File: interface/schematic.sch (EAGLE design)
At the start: 31 parts, among them J1 AUDIO_JACK_3.5MM_KIT, J2 AUDIO_JACK_3.5MM_KIT, J3 RJ45, T1 2N3904, T2 2N3904

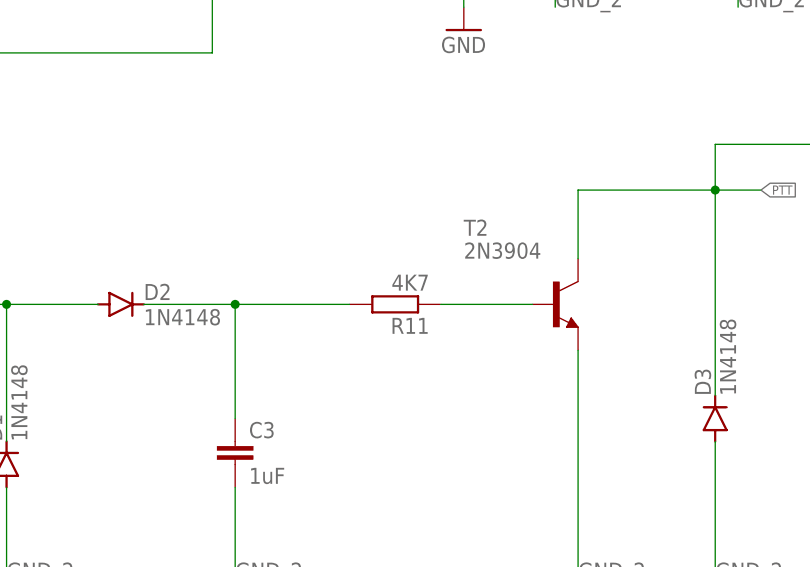
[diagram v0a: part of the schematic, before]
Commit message: Added decals
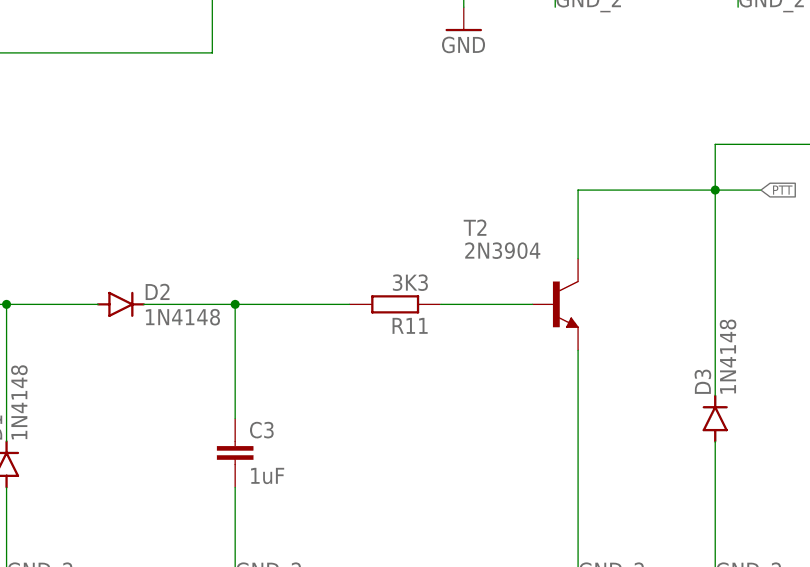
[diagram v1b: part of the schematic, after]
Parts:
- R11: value 4K7 -> 3K3
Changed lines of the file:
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@@
 <part name="R9" library="rcl" library_urn="urn:adsk.eagle:library:334" deviceset="R-EU_" device="0207/10" package3d_urn="urn:adsk.eagle:package:23491/2" value="330K"/>
 <part name="R10" library="rcl" library_urn="urn:adsk.eagle:library:334" deviceset="R-EU_" device="0207/10" package3d_urn="urn:adsk.eagle:package:23491/2" value="4K7"/>
-<part name="R11" library="rcl" library_urn="urn:adsk.eagle:library:334" deviceset="R-EU_" device="0207/10" package3d_urn="urn:adsk.eagle:package:23491/2" value="4K7"/>
+<part name="R11" library="rcl" library_urn="urn:adsk.eagle:library:334" deviceset="R-EU_" device="0207/10" package3d_urn="urn:adsk.eagle:package:23491/2" value="3K3"/>
 <part name="R13" library="rcl" library_urn="urn:adsk.eagle:library:334" deviceset="R-EU_" device="0207/10" package3d_urn="urn:adsk.eagle:package:23491/2" value="4k7"/>
 <part name="R5" library="rcl" library_urn="urn:adsk.eagle:library:334" deviceset="R-EU_" device="0207/10" package3d_urn="urn:adsk.eagle:package:23491/2" value="680R"/>

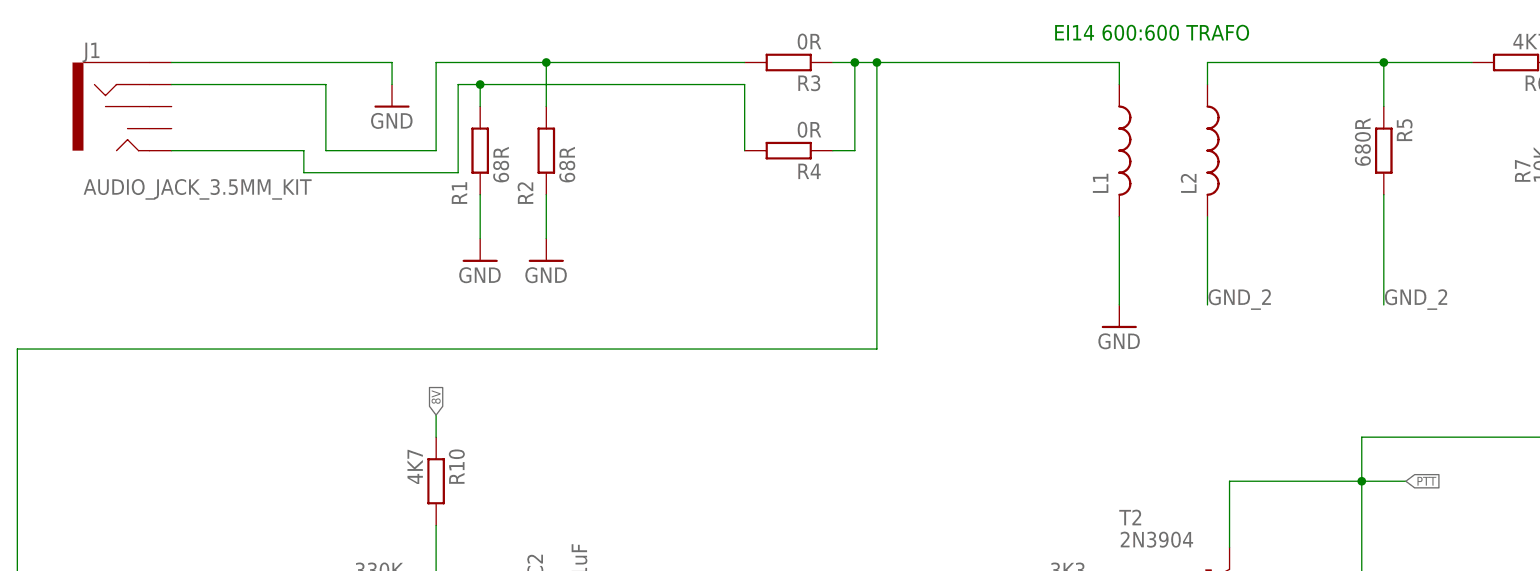
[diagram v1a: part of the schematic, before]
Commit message: Fixed component numbering to match ordered boards
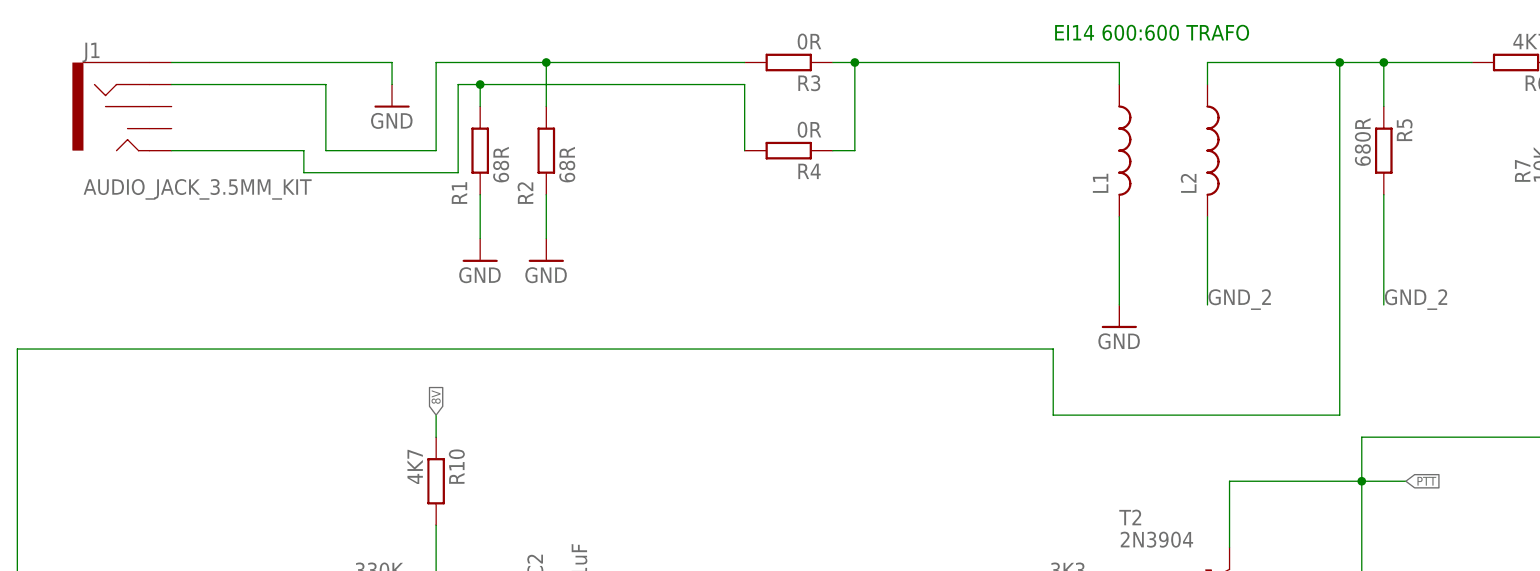
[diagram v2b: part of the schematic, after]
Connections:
- removed net N$8: L2.1, R5.1, R6.2
- new net N$16: L1.1, R3.1, R4.1
- net N$15: now also L2.1, R5.1, R6.2; no longer L1.1, R3.1, R4.1
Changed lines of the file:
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@@
-</segment>
-</net>
-<net name="N$8" class="0">
-<segment>
-<pinref part="L2" gate="G$1" pin="1"/>
-<wire x1="142.24" y1="167.64" x2="142.24" y2="170.18" width="0.1524" layer="91"/>
-<wire x1="142.24" y1="170.18" x2="162.56" y2="170.18" width="0.1524" layer="91"/>
-<pinref part="R6" gate="G$1" pin="2"/>
-<pinref part="R5" gate="G$1" pin="1"/>
-<wire x1="162.56" y1="170.18" x2="172.72" y2="170.18" width="0.1524" layer="91"/>
-<wire x1="162.56" y1="165.1" x2="162.56" y2="170.18" width="0.1524" layer="91"/>
-<junction x="162.56" y="170.18"/>
 </segment>
 </net>
@@
 <net name="N$15" class="0">
 <segment>
-<pinref part="L1" gate="G$1" pin="1"/>
-<wire x1="132.08" y1="170.18" x2="132.08" y2="167.64" width="0.1524" layer="91"/>
-<pinref part="R3" gate="G$1" pin="1"/>
-<wire x1="99.06" y1="170.18" x2="101.6" y2="170.18" width="0.1524" layer="91"/>
-<wire x1="101.6" y1="170.18" x2="104.14" y2="170.18" width="0.1524" layer="91"/>
-<pinref part="R4" gate="G$1" pin="1"/>
-<wire x1="99.06" y1="160.02" x2="101.6" y2="160.02" width="0.1524" layer="91"/>
-<wire x1="101.6" y1="160.02" x2="101.6" y2="170.18" width="0.1524" layer="91"/>
-<junction x="101.6" y="170.18"/>
-<wire x1="104.14" y1="170.18" x2="104.14" y2="137.16" width="0.1524" layer="91"/>
-<wire x1="104.14" y1="137.16" x2="5.08" y2="137.16" width="0.1524" layer="91"/>
+<wire x1="124.46" y1="137.16" x2="5.08" y2="137.16" width="0.1524" layer="91"/>
 <wire x1="5.08" y1="137.16" x2="5.08" y2="91.44" width="0.1524" layer="91"/>
 <pinref part="C1" gate="G$1" pin="1"/>
 <wire x1="5.08" y1="91.44" x2="10.16" y2="91.44" width="0.1524" layer="91"/>
-<wire x1="132.08" y1="170.18" x2="104.14" y2="170.18" width="0.1524" layer="91"/>
-<junction x="104.14" y="170.18"/>
+<wire x1="124.46" y1="137.16" x2="124.46" y2="129.54" width="0.1524" layer="91"/>
+<pinref part="L2" gate="G$1" pin="1"/>
+<wire x1="142.24" y1="167.64" x2="142.24" y2="170.18" width="0.1524" layer="91"/>
+<wire x1="142.24" y1="170.18" x2="157.48" y2="170.18" width="0.1524" layer="91"/>
+<pinref part="R6" gate="G$1" pin="2"/>
+<pinref part="R5" gate="G$1" pin="1"/>
+<wire x1="157.48" y1="170.18" x2="162.56" y2="170.18" width="0.1524" layer="91"/>
+<wire x1="162.56" y1="170.18" x2="172.72" y2="170.18" width="0.1524" layer="91"/>
+<wire x1="162.56" y1="165.1" x2="162.56" y2="170.18" width="0.1524" layer="91"/>
+<junction x="162.56" y="170.18"/>
+<wire x1="124.46" y1="129.54" x2="157.48" y2="129.54" width="0.1524" layer="91"/>
+<wire x1="157.48" y1="129.54" x2="157.48" y2="170.18" width="0.1524" layer="91"/>
+<junction x="157.48" y="170.18"/>
 </segment>
 </net>
@@
 </segment>
 </net>
+<net name="N$16" class="0">
+<segment>
+<pinref part="R3" gate="G$1" pin="1"/>
+<wire x1="99.06" y1="170.18" x2="101.6" y2="170.18" width="0.1524" layer="91"/>
+<junction x="101.6" y="170.18"/>
+<pinref part="L1" gate="G$1" pin="1"/>
+<wire x1="132.08" y1="170.18" x2="132.08" y2="167.64" width="0.1524" layer="91"/>
+<wire x1="132.08" y1="170.18" x2="101.6" y2="170.18" width="0.1524" layer="91"/>
+<wire x1="101.6" y1="160.02" x2="101.6" y2="170.18" width="0.1524" layer="91"/>
+<pinref part="R4" gate="G$1" pin="1"/>
+<wire x1="99.06" y1="160.02" x2="101.6" y2="160.02" width="0.1524" layer="91"/>
+</segment>
+</net>
